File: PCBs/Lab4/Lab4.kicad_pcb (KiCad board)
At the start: 2 copper layers, 13 parts, among them IC1 M0C1103QDDFRQ1, J1 Conn_01x05_Pin, SW1 SW_SPST, SW2 SW_SPST

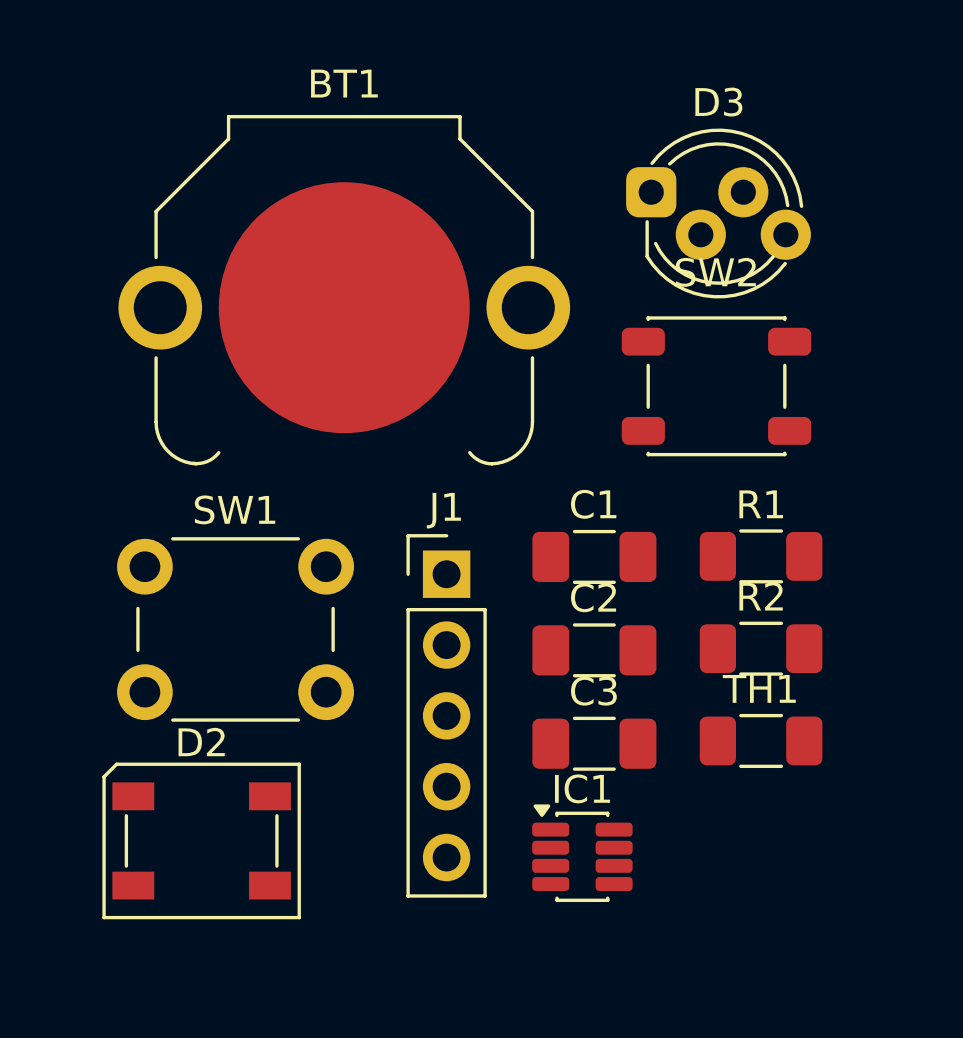
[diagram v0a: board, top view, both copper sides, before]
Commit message: Complete Labs 1-6: firmware and PCB submissions
Labs 1-3: GPIO/state machine LED control with button input
Lab 4: KiCad Simon PCB design
Lab 5: PWM buzzer + Mary Had a Little Lamb state machine
Lab 6: SPI RGB LED control synchronized to song and button presses
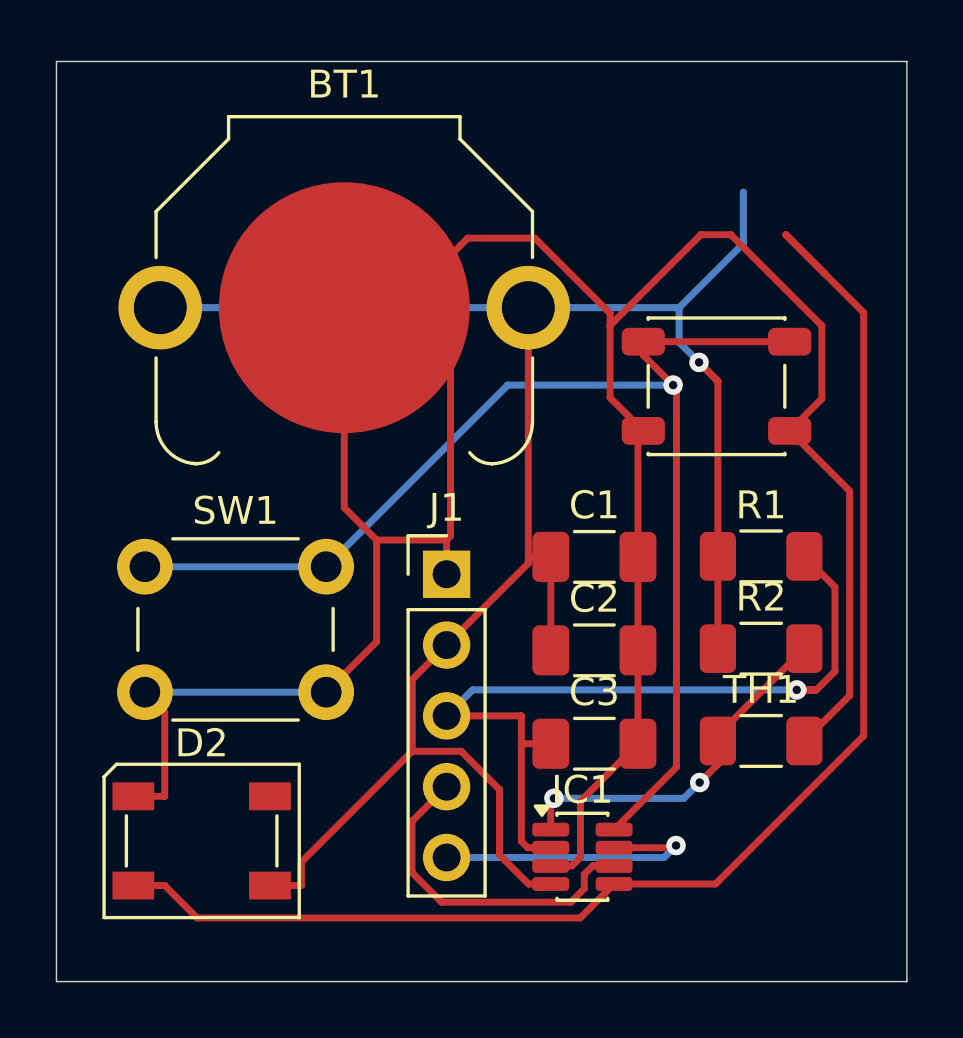
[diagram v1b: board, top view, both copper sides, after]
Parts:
- removed D3: NeoPixel_THT, LED_THT:LED_D5.0mm-4_RGB_Staggered_Pins
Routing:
- net GND: track 0.00 -> 97.1 mm
- net VDD: track 0.00 -> 76.1 mm, vias 0 -> 1
- net LED_DIN: track 0.00 -> 50.5 mm
- net Button: track 0.00 -> 45.8 mm, vias 0 -> 1
- net NRST: track 0.00 -> 30.0 mm, vias 0 -> 1
- net THRM: track 0.00 -> 13.3 mm, vias 0 -> 2
- net SWDIO: track 0.00 -> 12.1 mm
- net SWCLK: track 0.00 -> 10.9 mm, vias 0 -> 1
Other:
- board outline added: 30.5 x 33 mm
